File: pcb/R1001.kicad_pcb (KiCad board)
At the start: 4 copper layers, 45 x 33.3 mm, 39 parts, among them J1 PCIEXPRESS-X1, J2 CONN_01X04, J3 CONN127P-02X02, Q1 Q_NMOS_GSD, U1 DRV8825, U2 74LS157, U3 EFM8BB10F2G, U4 ZXCT1107

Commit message: layout wip
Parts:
- C9, R2: moved to B.Cu
- moved R18 30.6 mm to (151.4, 88.7), turned to 90 degrees
- moved R15 24.9 mm to (157.3, 89.5), turned to 90 degrees
- moved U4 21.6 mm to (154.0, 89.5), turned to 90 degrees
- moved C9 1.21 mm to (157.6, 88.1), turned to 90 degrees
- moved R2 0.85 mm to (155.4, 88.3), turned to 180 degrees
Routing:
- net HT: track 14.0 -> 16.5 mm
- net /HT_CON: track 22.1 -> 24.6 mm
- net /IVDD_SENSE: track 1.62 -> 3.24 mm
- net /D_VREF: track 5.62 -> 6.28 mm, vias 1 -> 0

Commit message: ready for v1.0.3 release
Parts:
- J3: value CONN127P-02X02 -> CONN_01X03; footprint Main:CONN127P-02X02 -> Main:SOCKET254P-01X03
- Q1, R19, R20, R21: moved to B.Cu
- moved R20 39.3 mm to (143.4, 78.5), turned to 180 degrees
- moved R21 37.3 mm to (139.2, 78.5), turned to 180 degrees
- moved Q1 35.0 mm to (135.9, 79.5), turned to 180 degrees
- moved R8 22.9 mm to (138.6, 91.7), turned to 270 degrees
- moved R19 18.6 mm to (138.6, 91.7), turned to 90 degrees
- moved R7 3.79 mm to (144.1, 75.7), turned to 0 degrees
- moved J3 2.72 mm to (148.3, 71.7), turned to 180 degrees
- moved R5 1.00 mm to (161.0, 86.0)
- moved R9 1.00 mm to (161.0, 78.0)
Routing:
- net PX2_~ENBL: track 2.30 -> 40.6 mm, vias 0 -> 2
- net PX3_STEP: track 4.13 -> 41.5 mm, vias 0 -> 2
- net ~MRESET: track 7.89 -> 38.4 mm, vias 1 -> 2
- net C2D: track 15.0 -> 37.3 mm
- net /DIR: track 15.2 -> 31.0 mm
- net /~MRESET_CON: track 24.7 -> 11.0 mm, vias 1 -> 0
- net /~ENBL: track 24.8 -> 37.9 mm
- net HT: track 16.5 -> 28.4 mm, vias 2 -> 6
- net /~D1_FAULT: track 8.07 -> 19.6 mm, vias 1 -> 2
- net /IVDD_SENSE: track 3.24 -> 12.3 mm, vias 0 -> 2
- net Net-(Q1-Pad3): track 0.00 -> 2.53 mm
- net /C2D_CON: track 13.4 -> 11.0 mm
- net /~D1_HOME: track 13.4 -> 15.7 mm
- net /STEP: track 33.0 -> 34.7 mm, vias 4 -> 3
- net +3V3: track 68.8 -> 69.9 mm, vias 7 -> 9
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- added copper zone on F.Cu, net /HT_CON
- added copper zone on In1.Cu, net HT
- added copper zone on In2.Cu, net HT
- removed copper zone on In2.Cu, net GND
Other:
- board text added: "C2D"
- board text added: "Debug"
- board text added: "R1001A v1.0.3 DRV8825 Stepper Motor Driver http://plugg.ee"
- board text added: "~RST"
- board text removed: "R1001A v1.0.2-beta DRV8825 Stepper Motor Driver http://plugg.ee"

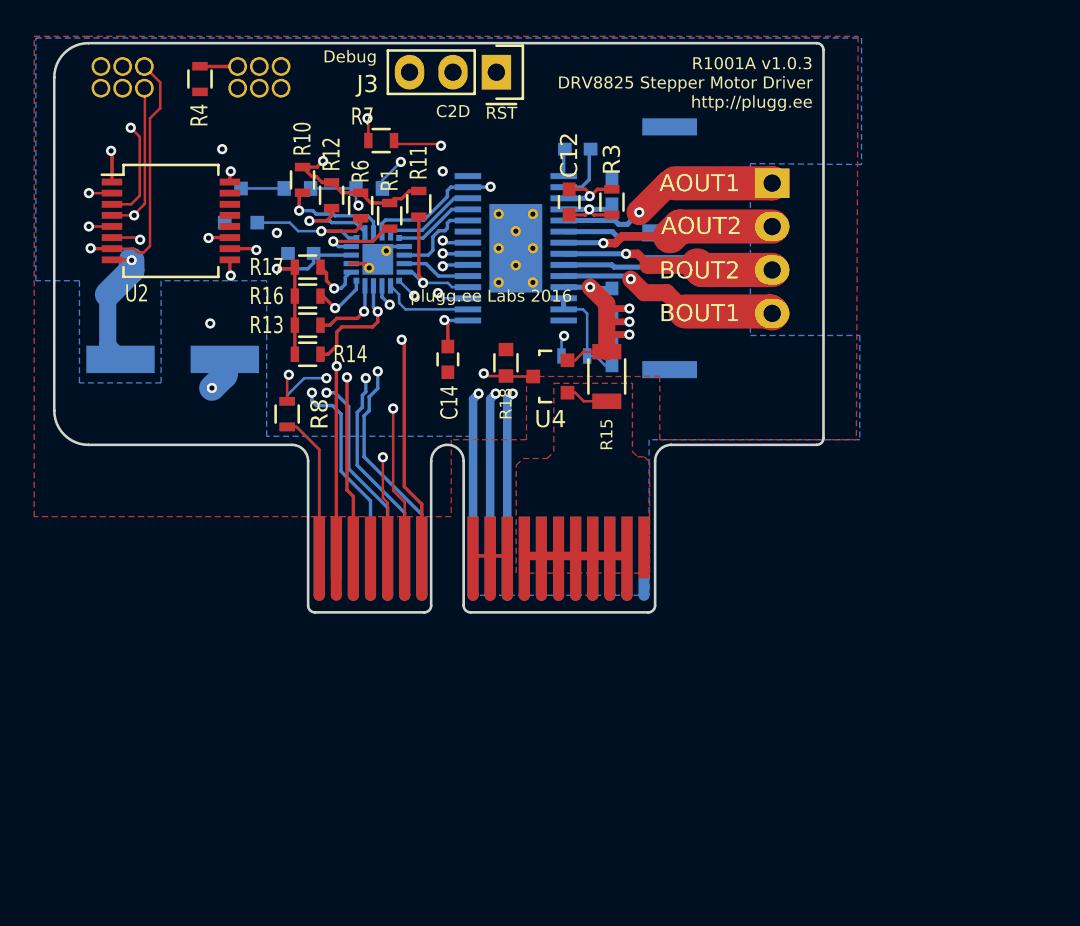
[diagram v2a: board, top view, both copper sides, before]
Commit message: added silk screen, fixed SOP footprint for pin 1 silkscreen, fixed 50mil connector drill size
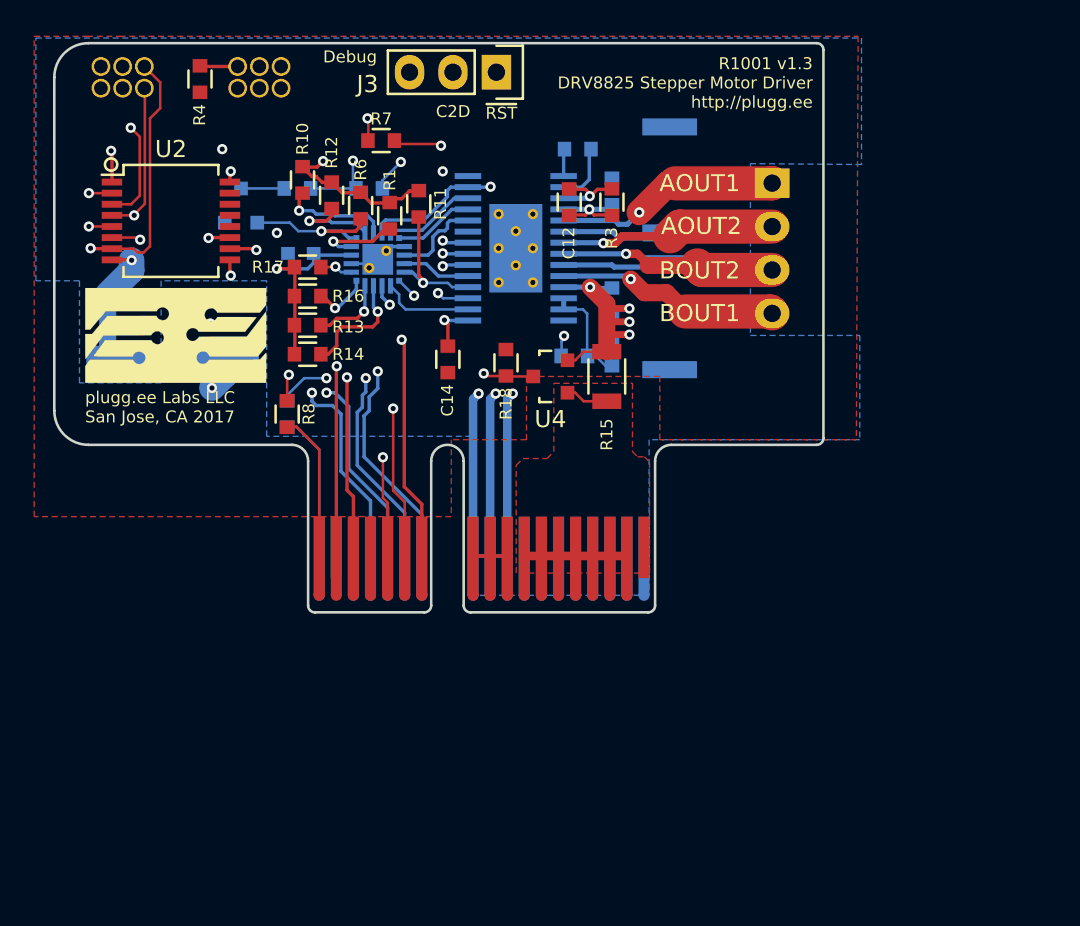
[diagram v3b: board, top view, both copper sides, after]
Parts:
- added A1: ART, pluggee:pluggeeLabsIcon-11x6, F.Cu at (132.1, 87.1)
- C10: value 0.01uF -> CC0603KRX7R9BB103; footprint Capacitors_SMD:C_0603 -> Main:CAPC0603
- C12, C5, C7: value 0.1uF -> CC0603KRX7R9BB104; footprint Capacitors_SMD:C_0603 -> Main:CAPC0603
- C14: value 1uF -> CC0603KRX5R6BB105; footprint Capacitors_SMD:C_0603 -> Main:CAPC0603
- C9: value 0.1uF -> CC0603KRX5R6BB105; footprint Capacitors_SMD:C_0603 -> Main:CAPC0603
- R1, R10, R11, R12, R13, R14, R16, R17, R4, R6, R7: value 10k -> RC0603FR-0710KL; footprint Resistors_SMD:R_0603 -> Main:RESC0603
- R15: value R1206 -> ERJ-8CWFR050V
- R18: value R0603 -> RC0603FR-072K8L
- R19, R8: value 1k -> RC0603FR-071KL; footprint Resistors_SMD:R_0603 -> Main:RESC0603
- R2: value 1M -> RC0603FR-0710KL; footprint Resistors_SMD:R_0603 -> Main:RESC0603
- R20: value R0603 -> RC0603FR-0715KL
- R21: value R0603 -> RC0603FR-0710KL
- R3: value 1M -> RC0603FR-071ML; footprint Resistors_SMD:R_0603 -> Main:RESC0603
- R5, R9: value 0.25 -> RHC2512FTR250; footprint Resistors_SMD:R_2512 -> Main:RESC2512
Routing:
- net /~D1_FAULT: track 19.6 -> 21.7 mm
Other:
- board text added: "R1001 v1.3 DRV8825 Stepper Motor Driver http://plugg.ee"
- board text added: "plugg.ee Labs LLC San Jose, CA 2017"
- board text removed: "R1001A v1.0.3 DRV8825 Stepper Motor Driver http://plugg.ee"
- board text removed: "plugg.ee Labs 2016"

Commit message: recreated gerbers, cleaned up BOM
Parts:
- added FID1: FIDTOP001, Main:FIDTOP001, F.Cu at (126.6, 75.5)
- added FID2: FIDTOP001, Main:FIDTOP001, B.Cu at (126.6, 75.5)
- added FID3: FIDTOP001, Main:FIDTOP001, F.Cu at (167.6, 91.2)
- added FID4: FIDTOP001, Main:FIDTOP001, B.Cu at (167.6, 91.2)
- C1: value 1uF -> CC0603KRX7R9BB104; footprint Capacitors_SMD:C_0603 -> Main:CAPC0603
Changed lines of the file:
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@@
     (tracks 615)
     (zones 0)
-    (modules 40)
+    (modules 44)
     (nets 49)
   )
   (page A4)
   (layers
-    (0 F.Cu power)
-    (1 In1.Cu signal)
-    (2 In2.Cu signal)
+    (0 F.Cu power hide)
+    (1 In1.Cu signal hide)
+    (2 In2.Cu signal hide)
     (31 B.Cu power)
     (32 B.Adhes user)
@@
     (35 F.Paste user)
     (36 B.SilkS user)
-    (37 F.SilkS user hide)
+    (37 F.SilkS user)
     (38 B.Mask user)
     (39 F.Mask user hide)
@@
     (pad_to_mask_clearance 0)
     (aux_axis_origin 0 0)
-    (visible_elements FFFEBFFF)
+    (visible_elements FFFEFFFF)
     (pcbplotparams
       (layerselection 0x010fc_80000007)
@@
       (net 45 /HT_CON) (zone_connect 2))
   )
-  (module Capacitors_SMD:C_0603 (layer B.Cu)
-    (at 139.425 82.3 180)
-    (descr "Capacitor SMD 0603, reflow soldering, AVX (see smccp.pdf)")
-    (tags "capacitor 0603")
-    (attr smd)
-    (fp_text reference C1 (at 2.5 0 180) (layer B.SilkS)
-      (effects (font (size 1 0.75) (thickness 0.15)) (justify mirror))
-    )
-    (fp_text value 1uF (at 0 -1.9 180) (layer B.Fab)
-      (effects (font (size 1 0.75) (thickness 0.15)) (justify mirror))
-    )
-    (fp_line (start -1.45 0.75) (end 1.45 0.75) (layer B.CrtYd) (width 0.05))
-    (fp_line (start -1.45 -0.75) (end 1.45 -0.75) (layer B.CrtYd) (width 0.05))
-    (fp_line (start -1.45 0.75) (end -1.45 -0.75) (layer B.CrtYd) (width 0.05))
-    (fp_line (start 1.45 0.75) (end 1.45 -0.75) (layer B.CrtYd) (width 0.05))
-    (fp_line (start -0.35 0.6) (end 0.35 0.6) (layer B.SilkS) (width 0.15))
-    (fp_line (start 0.35 -0.6) (end -0.35 -0.6) (layer B.SilkS) (width 0.15))
-    (pad 1 smd rect (at -0.75 0 180) (size 0.8 0.75) (layers B.Cu B.Paste B.Mask)
-      (net 2 +3V3))
-    (pad 2 smd rect (at 0.75 0 180) (size 0.8 0.75) (layers B.Cu B.Paste B.Mask)
-      (net 1 GND))
-    (model Capacitors_SMD.3dshapes/C_0603.wrl
-      (at (xyz 0 0 0))
-      (scale (xyz 1 1 1))
-      (rotate (xyz 0 0 0))
-    )
-  )
   (module Main:SOCKET254P-01X04 (layer B.Cu)
     (at 167 82 270)
@@
   (module Main:SOCKET127P-02X03 (layer B.Cu)
     (at 137 72 180)
-    (fp_text reference JSLAVE1 (at 0 -2.6 180) (layer B.SilkS)
-      (effects (font (size 1 1) (thickness 0.15)) (justify mirror))
+    (fp_text reference JSLAVE1 (at -2.7 -0.4 270) (layer B.SilkS)
+      (effects (font (size 0.7 0.7) (thickness 0.13)) (justify mirror))
     )
     (fp_text value SOCKMALE_02x03 (at 0 1.4 180) (layer B.Fab)
@@
   (module Main:SOCKET127P-02X03 (layer B.Cu)
     (at 129 72 180)
-    (fp_text reference JMASTER1 (at 0 -2.6 180) (layer B.SilkS)
-      (effects (font (size 1 1) (thickness 0.15)) (justify mirror))
+    (fp_text reference JMASTER1 (at -2.7 -0.8 270) (layer B.SilkS)
+      (effects (font (size 0.7 0.7) (thickness 0.13)) (justify mirror))
     )
     (fp_text value SOCKMALE_02x03 (at 0 1.4 180) (layer B.Fab)
@@
     (tags "SSOP 0.65")
     (attr smd)
-    (fp_text reference U2 (at 0 -4.2) (layer F.SilkS)
+    (fp_text reference U2 (at -5.325 -2.7) (layer F.SilkS)
       (effects (font (size 1 1) (thickness 0.15)))
     )
@@
       (xy 5.291667 -1.781631)) (layer F.SilkS) (width 0.01))
   )
+  (module Main:CAPC0603 (layer B.Cu)
+    (at 139.425 82.3 180)
+    (descr "Resistor SMD 0603, reflow soldering, Vishay (see dcrcw.pdf)")
+    (tags "resistor 0603")
+    (attr smd)
+    (fp_text reference C1 (at 0 1.27 180) (layer B.SilkS)
+      (effects (font (size 0.7 0.7) (thickness 0.15)) (justify mirror))
+    )
+    (fp_text value CC0603KRX7R9BB104 (at 0 -0.508 180) (layer B.Fab)
+      (effects (font (size 0.127 0.127) (thickness 0.03)) (justify mirror))
+    )
+    (fp_line (start -1.3 0.8) (end 1.3 0.8) (layer B.CrtYd) (width 0.05))
+    (fp_line (start -1.3 -0.8) (end 1.3 -0.8) (layer B.CrtYd) (width 0.05))
+    (fp_line (start -1.3 0.8) (end -1.3 -0.8) (layer B.CrtYd) (width 0.05))
+    (fp_line (start 1.3 0.8) (end 1.3 -0.8) (layer B.CrtYd) (width 0.05))
+    (fp_line (start 0.5 -0.675) (end -0.5 -0.675) (layer B.SilkS) (width 0.15))
+    (fp_line (start -0.5 0.675) (end 0.5 0.675) (layer B.SilkS) (width 0.15))
+    (pad 1 smd rect (at -0.7745 0 180) (size 0.787 0.864) (layers B.Cu B.Paste B.Mask)
+      (net 2 +3V3))
+    (pad 2 smd rect (at 0.7745 0 180) (size 0.787 0.864) (layers B.Cu B.Paste B.Mask)
+      (net 1 GND))
+    (model main.3dshapes/CAPC0603.wrl
+      (at (xyz 0 0 0))
+      (scale (xyz 1 1 1))
+      (rotate (xyz 0 0 0))
+    )
+  )
+  (module Main:FIDTOP001 (layer F.Cu)
+    (at 126.6 75.5)
+    (descr "Circular Fiducial, 1mm bare copper top; 2.54mm keepout")
+    (tags marker)
+    (attr virtual)
+    (fp_text reference FID1 (at 2.7 0.1) (layer F.SilkS) hide
+      (effects (font (size 0.7 0.7) (thickness 0.15)))
+    )
+    (fp_text value FIDTOP001 (at 0 -1.8) (layer F.Fab) hide
+      (effects (font (size 0.127 0.127) (thickness 0.03)))
+    )
+    (fp_circle (center 0 0) (end 1.55 0) (layer F.CrtYd) (width 0.05))
+    (pad ~ smd circle (at 0 0) (size 1 1) (layers F.Cu F.Mask)
+      (solder_mask_margin 0.77) (clearance 0.77))
+  )
+  (module Main:FIDTOP001 (layer F.Cu)
+    (at 167.6 91.2)
+    (descr "Circular Fiducial, 1mm bare copper top; 2.54mm keepout")
+    (tags marker)
+    (attr virtual)
+    (fp_text reference FID3 (at -2.4 1.6) (layer F.SilkS) hide
+      (effects (font (size 0.7 0.7) (thickness 0.15)))
+    )
+    (fp_text value FIDTOP001 (at 0 -1.8) (layer F.Fab) hide
+      (effects (font (size 0.127 0.127) (thickness 0.03)))
+    )
+    (fp_circle (center 0 0) (end 1.55 0) (layer F.CrtYd) (width 0.05))
+    (pad ~ smd circle (at 0 0) (size 1 1) (layers F.Cu F.Mask)
+      (solder_mask_margin 0.77) (clearance 0.77))
+  )
+  (module Main:FIDTOP001 (layer B.Cu)
+    (at 126.6 75.5)
+    (descr "Circular Fiducial, 1mm bare copper top; 2.54mm keepout")
+    (tags marker)
+    (attr virtual)
+    (fp_text reference FID2 (at 0 2.2) (layer B.SilkS) hide
+      (effects (font (size 0.7 0.7) (thickness 0.15)) (justify mirror))
+    )
+    (fp_text value FIDTOP001 (at 0 1.8) (layer B.Fab) hide
+      (effects (font (size 0.127 0.127) (thickness 0.03)) (justify mirror))
+    )
+    (fp_circle (center 0 0) (end 1.55 0) (layer B.CrtYd) (width 0.05))
+    (pad ~ smd circle (at 0 0) (size 1 1) (layers B.Cu B.Mask)
+      (solder_mask_margin 0.77) (clearance 0.77))
+  )
+  (module Main:FIDTOP001 (layer B.Cu)
+    (at 167.6 91.2)
+    (descr "Circular Fiducial, 1mm bare copper top; 2.54mm keepout")
+    (tags marker)
+    (attr virtual)
+    (fp_text reference FID4 (at 0 -2.3) (layer B.SilkS) hide
+      (effects (font (size 0.7 0.7) (thickness 0.15)) (justify mirror))
+    )
+    (fp_text value FIDTOP001 (at 0 1.8) (layer B.Fab) hide
+      (effects (font (size 0.127 0.127) (thickness 0.03)) (justify mirror))
+    )
+    (fp_circle (center 0 0) (end 1.55 0) (layer B.CrtYd) (width 0.05))
+    (pad ~ smd circle (at 0 0) (size 1 1) (layers B.Cu B.Mask)
+      (solder_mask_margin 0.77) (clearance 0.77))
+  )
   (gr_text ~RST (at 150.225 74.1) (layer F.SilkS)

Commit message: fixed silk screen version to v1.1
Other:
- board text added: "R1001 v1.1 DRV8825 Stepper Motor Driver http://plugg.ee"
- board text removed: "R1001 v1.3 DRV8825 Stepper Motor Driver http://plugg.ee"
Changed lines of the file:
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@@
     (links 176)
     (no_connects 0)
-    (area 124.924999 69.924999 170.075001 103.375001)
+    (area 123.225 67.573799 172.225001 103.524461)
     (thickness 1.6)
     (drawings 31)
@@
     (effects (font (size 0.7 0.7) (thickness 0.15)) (justify left))
   )
-  (gr_text "R1001 v1.3\nDRV8825 Stepper Motor Driver\nhttp://plugg.ee" (at 169.375 72.325) (layer F.SilkS)
+  (gr_text "R1001 v1.1\nDRV8825 Stepper Motor Driver\nhttp://plugg.ee" (at 169.375 72.325) (layer F.SilkS)
     (effects (font (size 0.7 0.7) (thickness 0.15)) (justify right))
   )

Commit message: added extra FID, changed silkscreen version to 1.1.1
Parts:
- added FID5: FIDTOP001, Main:FIDTOP001, F.Cu at (167.6, 72.4)
- added FID6: FIDTOP001, Main:FIDTOP001, B.Cu at (167.6, 72.4)
- C3: value 100uF -> 47uF
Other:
- board text added: "R1001 v1.1.1 Stepper Motor Driver http://plugg.ee"
- board text removed: "R1001 v1.1 DRV8825 Stepper Motor Driver http://plugg.ee"
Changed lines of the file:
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@@
     (links 176)
     (no_connects 0)
-    (area 123.225 67.573799 172.225001 103.524461)
+    (area 124.924999 69.924999 170.075001 103.375001)
     (thickness 1.6)
     (drawings 31)
     (tracks 615)
     (zones 0)
-    (modules 44)
+    (modules 46)
     (nets 49)
   )
@@
     (descr "Through hole socket strip")
     (tags "socket strip")
-    (fp_text reference J2 (at -6.5 -0.025 270) (layer B.SilkS)
+    (fp_text reference J2 (at -6.5 -0.025 270) (layer B.SilkS) hide
       (effects (font (size 1 1) (thickness 0.15)) (justify mirror))
     )
@@
       (effects (font (size 1 1) (thickness 0.15)) (justify mirror))
     )
-    (fp_text value 100uF (at 0 -5.08) (layer B.Fab)
+    (fp_text value 47uF (at 0 -5.08) (layer B.Fab)
       (effects (font (size 1 1) (thickness 0.15)) (justify mirror))
     )
@@
     (descr "Through hole socket strip")
     (tags "socket strip")
-    (fp_text reference J3 (at 5 -0.7 180) (layer F.SilkS)
+    (fp_text reference J3 (at 5 -0.7 180) (layer F.SilkS) hide
       (effects (font (size 1 1) (thickness 0.15)))
     )
@@
       (solder_mask_margin 0.77) (clearance 0.77))
   )
+  (module Main:FIDTOP001 (layer F.Cu)
+    (at 167.6 72.4)
+    (descr "Circular Fiducial, 1mm bare copper top; 2.54mm keepout")
+    (tags marker)
+    (attr virtual)
+    (fp_text reference FID5 (at 0 2.3) (layer F.SilkS) hide
+      (effects (font (size 0.7 0.7) (thickness 0.15)))
+    )
+    (fp_text value FIDTOP001 (at 0 -1.8) (layer F.Fab) hide
+      (effects (font (size 0.127 0.127) (thickness 0.03)))
+    )
+    (fp_circle (center 0 0) (end 1.55 0) (layer F.CrtYd) (width 0.05))
+    (pad ~ smd circle (at 0 0) (size 1 1) (layers F.Cu F.Mask)
+      (solder_mask_margin 0.77) (clearance 0.77))
+  )
+  (module Main:FIDTOP001 (layer B.Cu)
+    (at 167.6 72.4)
+    (descr "Circular Fiducial, 1mm bare copper top; 2.54mm keepout")
+    (tags marker)
+    (attr virtual)
+    (fp_text reference FID6 (at 0 -2.3) (layer B.SilkS) hide
+      (effects (font (size 0.7 0.7) (thickness 0.15)) (justify mirror))
+    )
+    (fp_text value FIDTOP001 (at 0 1.8) (layer B.Fab) hide
+      (effects (font (size 0.127 0.127) (thickness 0.03)) (justify mirror))
+    )
+    (fp_circle (center 0 0) (end 1.55 0) (layer B.CrtYd) (width 0.05))
+    (pad ~ smd circle (at 0 0) (size 1 1) (layers B.Cu B.Mask)
+      (solder_mask_margin 0.77) (clearance 0.77))
+  )
   (gr_text ~RST (at 150.225 74.1) (layer F.SilkS)
     (effects (font (size 0.7 0.7) (thickness 0.15)) (justify left))
@@
     (effects (font (size 0.7 0.7) (thickness 0.15)) (justify left))
   )
-  (gr_text "R1001 v1.1\nDRV8825 Stepper Motor Driver\nhttp://plugg.ee" (at 169.375 72.325) (layer F.SilkS)
-    (effects (font (size 0.7 0.7) (thickness 0.15)) (justify right))
+  (gr_text "R1001 v1.1.1\nStepper Motor Driver\nhttp://plugg.ee" (at 153.4 71.95) (layer F.SilkS)
+    (effects (font (size 0.7 0.7) (thickness 0.15)) (justify left))
   )
   (gr_arc (start 169.6 70.4) (end 170 70.4) (angle -90) (layer Edge.Cuts) (width 0.15))

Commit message: fixed silk screen signal names
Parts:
- removed J3: CONN_01X03, Main:SOCKET254P-01X03
- added TP1: TestPoint, Main:TestPoint000, F.Cu at (148.0, 91.7)
- added TP2: TestPoint, Main:TestPoint000, F.Cu at (162.0, 91.7)
- added TP3: TestPoint, Main:TestPoint000, F.Cu at (130.3, 91.3)
- added TP4: TestPoint, Main:TestPoint000, F.Cu at (127.4, 91.3)
- J2: footprint Main:SOCKET254P-01X04 -> Main:70553-0038
- U3: value EFM8BB10F2G -> EFM8BB10F8G
- moved A1 24.4 mm to (152.3, 73.4)
- moved FID3 6.00 mm to (173.6, 91.2)
- moved FID4 6.00 mm to (173.6, 91.2)
- moved FID5 6.00 mm to (173.6, 72.4)
- moved FID6 6.00 mm to (173.6, 72.4)
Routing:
- net ~MRESET: track 38.4 -> 27.3 mm
- net C2D: track 37.3 -> 31.1 mm, vias 2 -> 3
- net +3V3: track 69.9 -> 72.2 mm
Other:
- board size 45 x 33.3 mm -> 51 x 33.3 mm
- board text added: "3.3V"
- board text added: "GND"
- board text added: "R1001 v1.1.2 Stepper Motor Driver http://plugg.ee plugg.ee Labs LLC, 2017 San Jose, CA, USA"
- board text added: "~MRESET"
- board text removed: "Debug"
- board text removed: "R1001 v1.1.1 Stepper Motor Driver http://plugg.ee"
- board text removed: "plugg.ee Labs LLC San Jose, CA 2017"
- board text removed: "~RST"

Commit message: read for version 1.1.2, crowdsupply build
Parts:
- removed R20: RC0603FR-0715KL, Main:RESC0603
- removed R21: RC0603FR-0710KL, Main:RESC0603
- added C112: CC0603KRX5R6BB105, Main:CAPC0603, F.Cu at (149.4, 85.9)
- added R120: RC0603FR-07100KL, Main:RESC0603, F.Cu at (149.4, 88.7)
- added R121: RC0603FR-07100KL, Main:RESC0603, F.Cu at (134.9, 74.8)
- R4: value RC0603FR-0710KL -> RC0603FR-072K8L
- moved C14 1.03 mm to (147.0, 88.5)
- moved R4 0.53 mm to (133.0, 72.1)
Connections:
- JSLAVE1 pad 6: /SLAVE_ENABLE -> /SLAVE_ENABLE_CON
- Q1 pad 3: Net-(Q1-Pad3) -> /SLAVE_ENABLE
- R18 pad 1: /IVDD_SENSE -> Net-(R120-Pad1)
- R4 pad 1: /SLAVE_ENABLE -> /SLAVE_ENABLE_CON
- R4 pad 2: GND -> /SLAVE_ENABLE
- U4 pad 3: /IVDD_SENSE -> Net-(R120-Pad1)
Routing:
- net /IVDD_SENSE: track 12.3 -> 6.65 mm, vias 2 -> 1
- net Net-(R120-Pad1): track 0.00 -> 3.64 mm
- net HT: track 28.4 -> 31.5 mm
- net /SLAVE_ENABLE_CON: track 0.00 -> 2.92 mm
- net Net-(Q1-Pad3): track 2.53 -> 0.00 mm
- net GND: track 29.8 -> 32.0 mm
- net +3V3: track 72.2 -> 70.2 mm, vias 9 -> 8
- net /SLAVE_ENABLE: track 15.9 -> 17.4 mm
- net /D1_ISENA: track 7.15 -> 6.48 mm
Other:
- board text added: "Master"
- board text added: "Slave"
